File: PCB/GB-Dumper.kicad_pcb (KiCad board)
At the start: 2 copper layers, 89.5 x 72 mm, 26 parts, among them J1 GameBoy_Cartridge_MountingPin, J2 Conn_01x03_Male, J3 Conn_01x02_Male, J4 Conn_01x04_Female, U1 74HC595, U2 74HC595

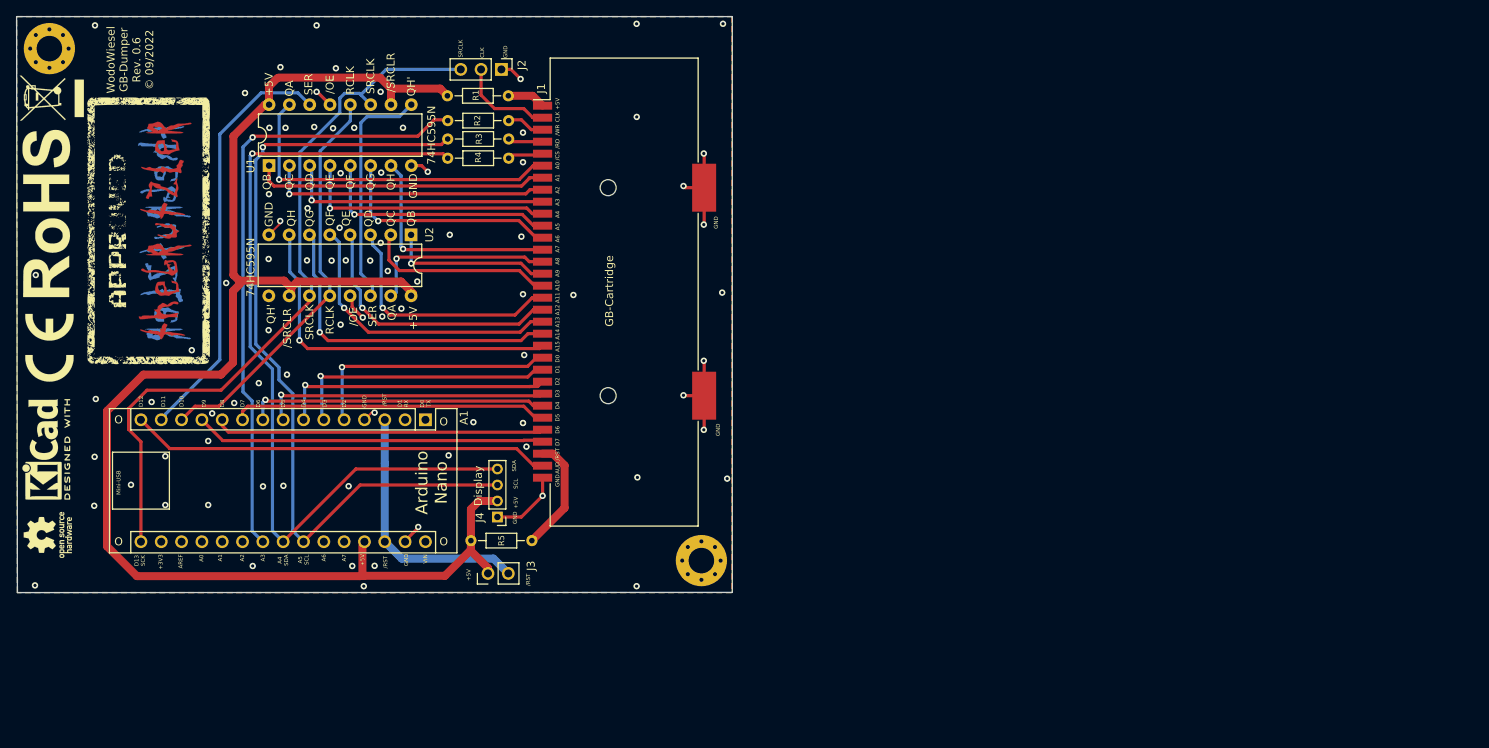
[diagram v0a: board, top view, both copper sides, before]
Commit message: -update design to 0.7 (clk 6 rst jumpers)
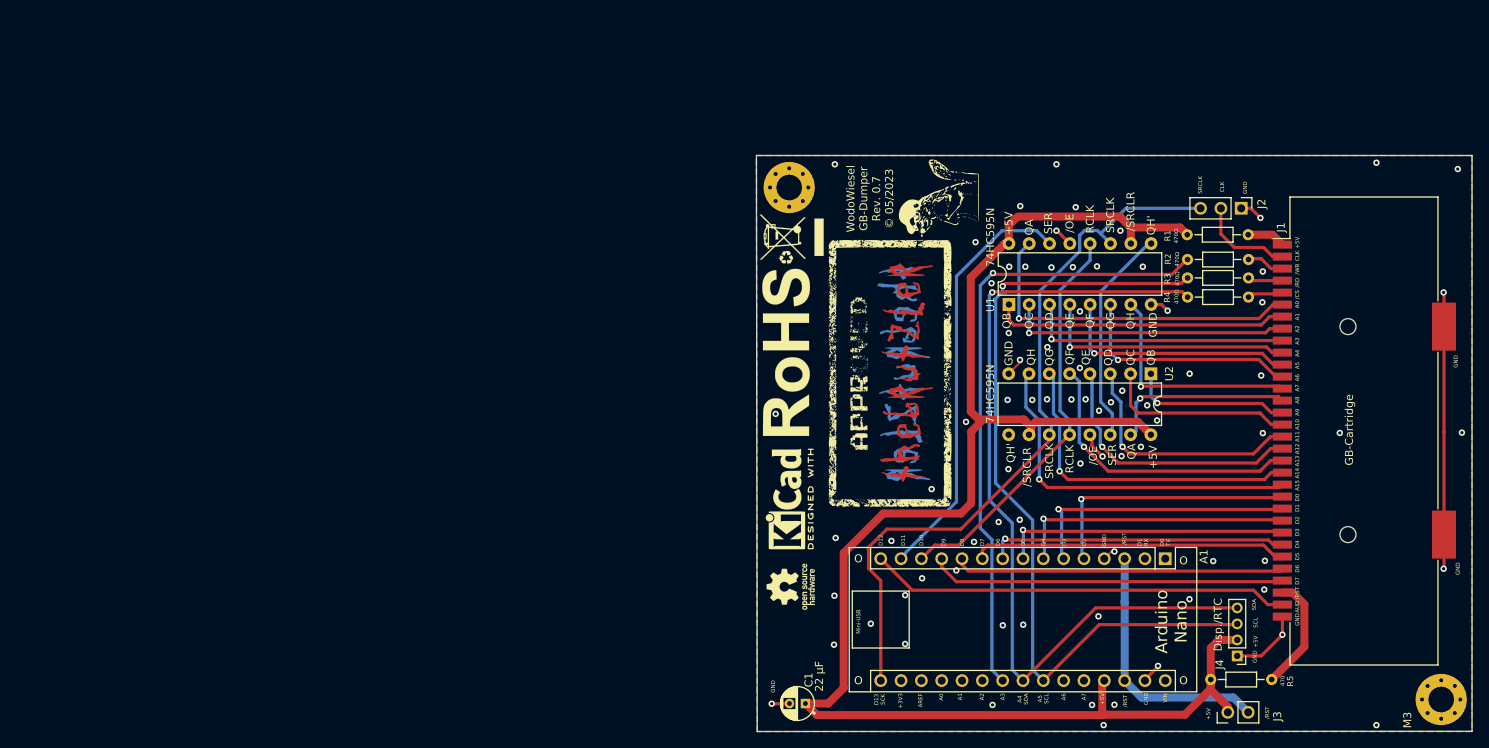
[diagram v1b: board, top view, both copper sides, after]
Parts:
- removed REF2*, REF3: CE-Logo_8.5x6mm_SilkScreen, Symbol:CE-Logo_8.5x6mm_SilkScreen
- added C1: 22 µF, Capacitor_THT:CP_Radial_D4.0mm_P2.00mm, F.Cu at (190.5, 152.1)
- added G2: LOGO, Logos:wiesel-kicad-back-white, F.Cu at (207.2, 89.1)
- added G2*: LOGO, Logos:wiesel-kicad-back-white, B.Cu at (207.2, 88.9)
- added G3: LOGO, Logos:recycling-symbol-kicad, F.Cu at (188.1, 96.3)
- added G3*: LOGO, Logos:recycling-symbol-kicad, B.Cu at (188.5, 96.3)
- R1, R2, R3, R4: value 470 -> 470Ω
- moved G1 94.4 mm to (201.1, 110.8)
- moved G2* 94.1 mm to (200.7, 110.6)
- moved J1 94.1 mm to (260.4, 117.9)
- moved J2 94.1 mm to (245.0, 90.2)
- moved J3 94.1 mm to (243.3, 153.2)
- moved J4 94.1 mm to (244.5, 146.1)
- moved R1 94.1 mm to (238.2, 93.5)
- moved R2 94.1 mm to (238.3, 96.6)
- moved R3 94.1 mm to (238.3, 98.9)
- moved R4 94.1 mm to (238.3, 101.3)
- moved R5 94.1 mm to (241.2, 149.1)
- moved REF3* 94.1 mm to (188.1, 108.2)
- moved REF4 94.1 mm to (188.1, 108.2)
- moved REF6 94.1 mm to (188.5, 87.6)
- moved REF7 94.1 mm to (270.0, 151.6)
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- renumbered G2 to G2*
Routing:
- net GND: track 49.9 -> 63.8 mm, vias 85 -> 78
- net Net-(A1-Pad27): track 188.0 -> 198.0 mm
- net Net-(U1-Pad9): track 29.5 -> 27.3 mm
- net Net-(A1-Pad12): track 43.8 -> 44.4 mm
- net Net-(A1-Pad6): track 33.8 -> 34.5 mm
- net Net-(A1-Pad5): track 32.2 -> 32.9 mm
- net Net-(A1-Pad22): track 77.4 -> 78.0 mm
- net Net-(A1-Pad7): track 34.5 -> 35.1 mm
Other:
- board text added: "22 µF"
- board text added: "470Ω"
- board text added: "C1"
- board text added: "Disp./RTC"
- board text added: "M3"
- board text added: "WodoWiesel GB-Dumper Rev. 0.7 © 05/2023"
- board text removed: "Display"
- board text removed: "WodoWiesel GB-Dumper Rev. 0.6 © 09/2022"

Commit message: -optimized resistors, caps, routing -cleanup folders/exports
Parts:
- renumbered G2* to G2**
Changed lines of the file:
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@@
       (sketchpadsonfab true)
       (subtractmaskfromsilk false)
-      (outputformat 4)
+      (outputformat 1)
       (mirror false)
       (drillshape 0)
       (scaleselection 1)
-      (outputdirectory "")
+      (outputdirectory "C:/github/GB-Dumper/PCB/gbr/")
     )
   )
@@
     (at 207.158 89.054 90)
     (attr board_only exclude_from_pos_files exclude_from_bom)
-    (fp_text reference "G2" (at -8.53 -10.87 90) (layer "User.1")
+    (fp_text reference "G2" (at -8.53 -10.87 90) (layer "B.Fab") hide
       (effects (font (size 1.524 1.524) (thickness 0.3)))
     )
@@
     (at 201.088 110.824 90)
     (attr through_hole)
-    (fp_text reference "G1" (at -12.827 -2.54 90) (layer "F.SilkS") hide
+    (fp_text reference "G1" (at -12.827 -2.54 90) (layer "B.Fab") hide
       (effects (font (size 1.524 1.524) (thickness 0.3)))
     )
-    (fp_text value "LOGO" (at -0.762 -1.27 90) (layer "F.SilkS") hide
+    (fp_text value "LOGO" (at -0.762 -1.27 90) (layer "B.Fab") hide
       (effects (font (size 1.524 1.524) (thickness 0.3)))
     )
@@
     (at 200.737406 110.595778 -90)
     (attr through_hole)
-    (fp_text reference "G2*" (at -21.431778 -2.950594 90) (layer "B.SilkS") hide
+    (fp_text reference "G2**" (at -21.431778 -2.950594 90) (layer "B.SilkS") hide
       (effects (font (size 1.524 1.524) (thickness 0.3)) (justify mirror))
     )
@@
     (pts (xy 184.368 83.584) (xy 273.858 83.554))
     (height -3.450234)
-    (gr_text "89,5 mm" (at 229.11124 78.318766 0.01920743458) (layer "Dwgs.User")
+    (gr_text "89.5 mm" (at 229.11124 78.318766 0.01920743458) (layer "Dwgs.User")
       (effects (font (size 1.5 1.5) (thickness 0.3)))
     )
@@
     (pts (xy 184.478 155.564) (xy 184.398 83.584))
     (height -6.807473)
-    (gr_text "72,0 mm" (at 178.78053 119.580288 -89.93632036) (layer "Dwgs.User")
+    (gr_text "72.0 mm" (at 178.78053 119.580288 -89.93632036) (layer "Dwgs.User")
       (effects (font (size 1 1) (thickness 0.15)))
     )

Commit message: fix typo
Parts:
- R5: value 470 -> 470Ω
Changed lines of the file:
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@@
       (effects (font (size 0.75 0.75) (thickness 0.15)))
     )
-    (fp_text value "470" (at 8.99 0.16 270) (layer "F.SilkS")
+    (fp_text value "470Ω" (at 8.99 0.16 270) (layer "F.SilkS")
       (effects (font (size 0.5 0.5) (thickness 0.125)))
     )

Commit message: -better gnd with mounting holes -cleanup silkscreen -removes orientation crosses -generated new gerbers/exports
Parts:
- removed REF3*, REF4: RoHS-Logo_6mm_SilkScreen, Symbol:RoHS-Logo_6mm_SilkScreen
- removed REF6, REF7: MountingHole_3.2mm_M3_Pad_Via, MountingHole:MountingHole_3.2mm_M3_Pad_Via
- added REF888**: MountingHole_3.2mm_M3_Pad, MountingHole:MountingHole_3.2mm_M3_Pad, F.Cu at (269.6, 151.5)
- added REF999**: MountingHole_3.2mm_M3_Pad, MountingHole:MountingHole_3.2mm_M3_Pad, F.Cu at (188.6, 87.7)
- moved REF1* 18.2 mm to (188.2, 109.1)
- moved REF2 17.4 mm to (187.9, 109.1)
- moved REF0 15.0 mm to (188.0, 122.5)
- moved REF0* 14.9 mm to (188.1, 122.5)
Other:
- board text added: "+"
- board text added: "RoHS HASL-LF"
